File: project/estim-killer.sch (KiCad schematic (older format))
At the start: 3 parts

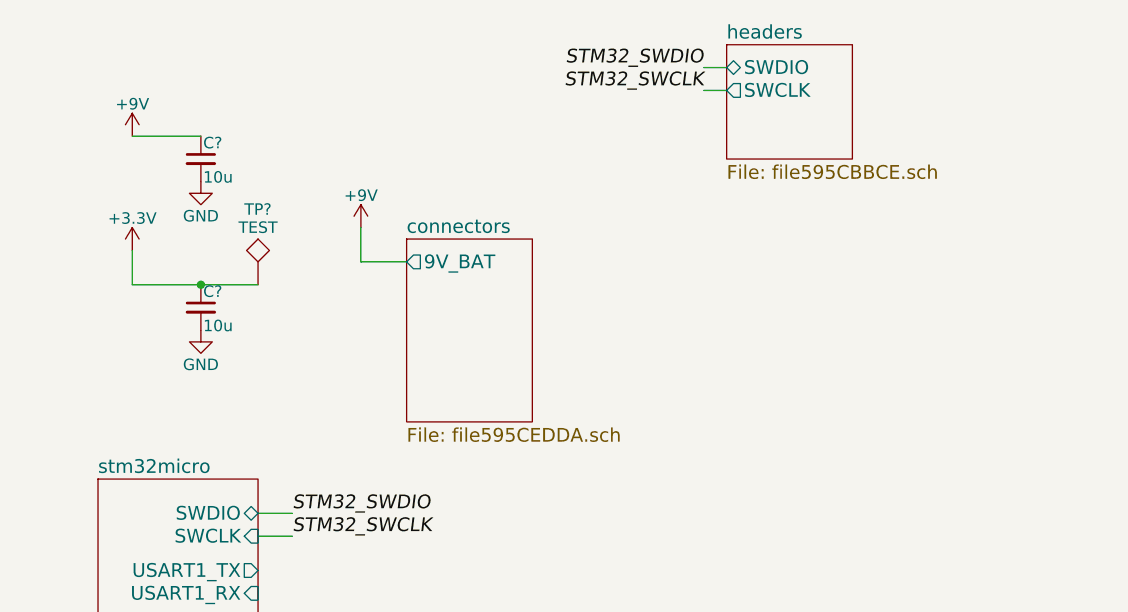
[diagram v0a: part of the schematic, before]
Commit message: Added 9V -> 3.3V buck regulator (TPS560200).
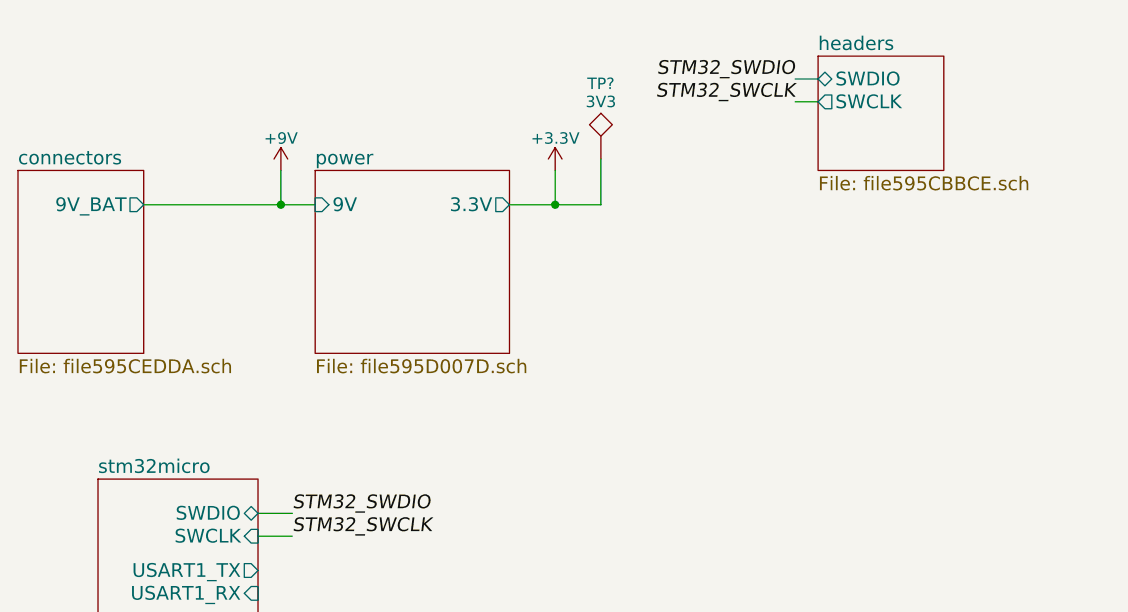
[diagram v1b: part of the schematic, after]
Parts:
- removed C?: 10u, Capacitors_SMD:C_0805, symbol C_Small
- removed C?: 10u, Capacitors_SMD:C_0603, symbol C_Small
- removed TP?: TEST, symbol TEST
- added TP?: 3V3, Measurement_Points:Measurement_Point_Round-SMD-Pad_Small, symbol TEST
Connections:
- net +3V3: now also TP?.1
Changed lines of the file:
@@
 LIBS:valves
 LIBS:estim-killer
+LIBS:estim-killer-cache
 EELAYER 25 0
 EELAYER END
 $Descr A4 11693 8268
 encoding utf-8
-Sheet 1 4
+Sheet 1 5
 Title ""
 Date ""
@@
 Comment4 ""
 $EndDescr
-$Comp
-L +9V #PWR?
-U 1 1 595C7B7C
-P 1350 1200
-F 0 "#PWR?" H 1350 1050 50  0001 C CNN
-F 1 "+9V" H 1350 1340 50  0000 C CNN
-F 2 "" H 1350 1200 50  0001 C CNN
-F 3 "" H 1350 1200 50  0001 C CNN
-	1    1350 1200
-	1    0    0    -1
-$EndComp
-$Comp
-L +3.3V #PWR?
-U 1 1 595C836F
-P 1350 1700
-F 0 "#PWR?" H 1350 1550 50  0001 C CNN
-F 1 "+3.3V" H 1350 1840 50  0000 C CNN
-F 2 "" H 1350 1700 50  0001 C CNN
-F 3 "" H 1350 1700 50  0001 C CNN
-	1    1350 1700
-	1    0    0    -1
-$EndComp
-$Comp
-L C_Small C?
-U 1 1 595C83A0
-P 1650 1300
-F 0 "C?" H 1660 1370 50  0000 L CNN
-F 1 "10u" H 1660 1220 50  0000 L CNN
-F 2 "Capacitors_SMD:C_0805" H 1650 1300 50  0001 C CNN
-F 3 "" H 1650 1300 50  0001 C CNN
-	1    1650 1300
-	1    0    0    -1
-$EndComp
-$Comp
-L GND #PWR?
-U 1 1 595C83DB
-P 1650 1400
-F 0 "#PWR?" H 1650 1150 50  0001 C CNN
-F 1 "GND" H 1650 1250 50  0000 C CNN
-F 2 "" H 1650 1400 50  0001 C CNN
-F 3 "" H 1650 1400 50  0001 C CNN
-	1    1650 1400
-	1    0    0    -1
-$EndComp
-Wire Wire Line
-	1350 1200 1650 1200
-$Comp
-L C_Small C?
-U 1 1 595C8416
-P 1650 1950
-F 0 "C?" H 1660 2020 50  0000 L CNN
-F 1 "10u" H 1660 1870 50  0000 L CNN
-F 2 "Capacitors_SMD:C_0603" H 1650 1950 50  0001 C CNN
-F 3 "" H 1650 1950 50  0001 C CNN
-	1    1650 1950
-	1    0    0    -1
-$EndComp
-Wire Wire Line
-	1350 1700 1350 1850
-Wire Wire Line
-	1350 1850 1900 1850
-$Comp
-L GND #PWR?
-U 1 1 595C8472
-P 1650 2050
-F 0 "#PWR?" H 1650 1800 50  0001 C CNN
-F 1 "GND" H 1650 1900 50  0000 C CNN
-F 2 "" H 1650 2050 50  0001 C CNN
-F 3 "" H 1650 2050 50  0001 C CNN
-	1    1650 2050
-	1    0    0    -1
-$EndComp
 $Sheet
 S 1200 2700 700  1350
@@
 $EndSheet
 $Sheet
-S 3950 800  550  500
+S 4350 850  550  500
 U 595CBBCF
 F0 "headers" 60
 F1 "file595CBBCE.sch" 60
-F2 "SWDIO" B L 3950 900 60
-F3 "SWCLK" O L 3950 1000 60
+F2 "SWDIO" B L 4350 950 60
+F3 "SWCLK" O L 4350 1050 60
 $EndSheet
-Text Label 3850 900  2    60   Italic 0
+Text Label 4250 950  2    60   Italic 0
 STM32_SWDIO
-Text Label 3850 1000 2    60   Italic 0
+Text Label 4250 1050 2    60   Italic 0
 STM32_SWCLK
 Wire Wire Line
-	3850 1000 3950 1000
+	4250 1050 4350 1050
 Wire Wire Line
-	3850 900  3950 900
+	4250 950  4350 950
 Text Label 2050 2850 0    60   Italic 0
 STM32_SWDIO
@@
 	1900 2950 2050 2950
 $Sheet
-S 2550 1650 550  800
+S 850  1350 550  800
 U 595CEDDB
 F0 "connectors" 60
 F1 "file595CEDDA.sch" 60
-F2 "9V_BAT" O L 2550 1750 60
+F2 "9V_BAT" O R 1400 1500 60
 $EndSheet
-$Comp
-L TEST TP?
-U 1 1 595CF833
-P 1900 1850
-F 0 "TP?" H 1900 2150 50  0000 C BNN
-F 1 "TEST" H 1900 2100 50  0000 C CNN
-F 2 "" H 1900 1850 50  0001 C CNN
-F 3 "" H 1900 1850 50  0001 C CNN
-	1    1900 1850
-	1    0    0    -1
-$EndComp
-Connection ~ 1650 1850
+$Sheet
+S 2150 1350 850  800
+U 595D007E
+F0 "power" 60
+F1 "file595D007D.sch" 60
+F2 "3.3V" O R 3000 1500 60
+F3 "9V" I L 2150 1500 60
+$EndSheet
+Wire Wire Line
+	1400 1500 2150 1500
 $Comp
 L +9V #PWR?
-U 1 1 595CFAF7
-P 2350 1600
-F 0 "#PWR?" H 2350 1450 50  0001 C CNN
-F 1 "+9V" H 2350 1740 50  0000 C CNN
-F 2 "" H 2350 1600 50  0001 C CNN
-F 3 "" H 2350 1600 50  0001 C CNN
-	1    2350 1600
+U 1 1 595D15BF
+P 2000 1350
+F 0 "#PWR?" H 2000 1200 50  0001 C CNN
+F 1 "+9V" H 2000 1490 50  0000 C CNN
+F 2 "" H 2000 1350 50  0001 C CNN
+F 3 "" H 2000 1350 50  0001 C CNN
+	1    2000 1350
 	1    0    0    -1
 $EndComp
 Wire Wire Line
-	2350 1600 2350 1750
+	2000 1350 2000 1500
+Connection ~ 2000 1500
+$Comp
+L +3.3V #PWR?
+U 1 1 595D18DD
+P 3200 1350
+F 0 "#PWR?" H 3200 1200 50  0001 C CNN
+F 1 "+3.3V" H 3200 1490 50  0000 C CNN
+F 2 "" H 3200 1350 50  0001 C CNN
+F 3 "" H 3200 1350 50  0001 C CNN
+	1    3200 1350
+	1    0    0    -1
+$EndComp
+$Comp
+L TEST TP?
+U 1 1 595D1C32
+P 3400 1300
+F 0 "TP?" H 3400 1600 50  0000 C BNN
+F 1 "3V3" H 3400 1550 50  0000 C CNN
+F 2 "Measurement_Points:Measurement_Point_Round-SMD-Pad_Small" H 3400 1300 50  0001 C CNN
+F 3 "" H 3400 1300 50  0001 C CNN
+	1    3400 1300
+	1    0    0    -1
+$EndComp
 Wire Wire Line
-	2350 1750 2550 1750
+	3000 1500 3400 1500
+Wire Wire Line
+	3400 1500 3400 1300
+Wire Wire Line
+	3200 1350 3200 1500
+Connection ~ 3200 1500
 $EndSCHEMATC

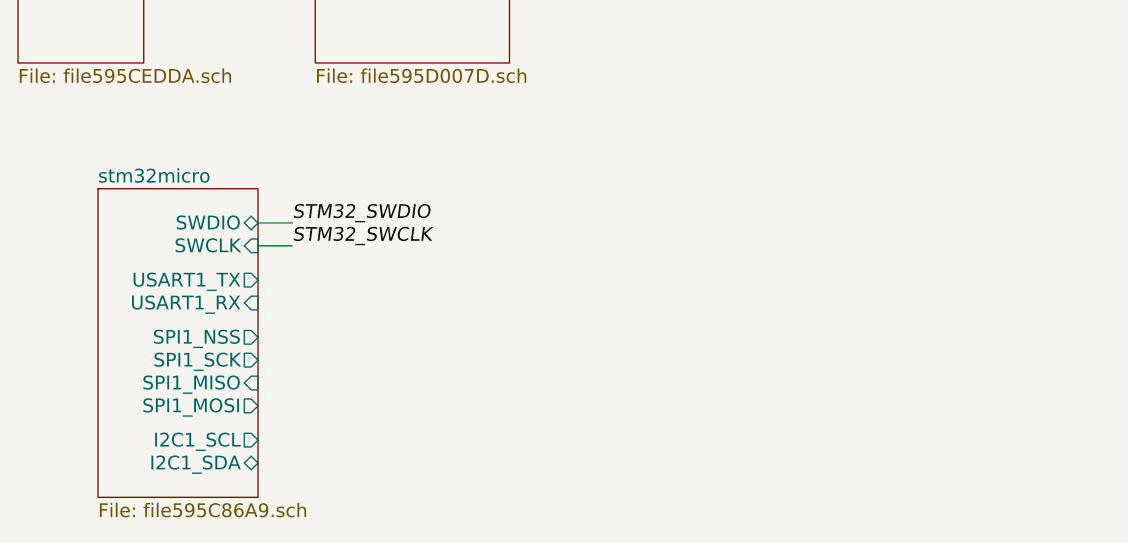
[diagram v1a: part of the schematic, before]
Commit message: Add AD5689R dual-channel DAC to schematic.
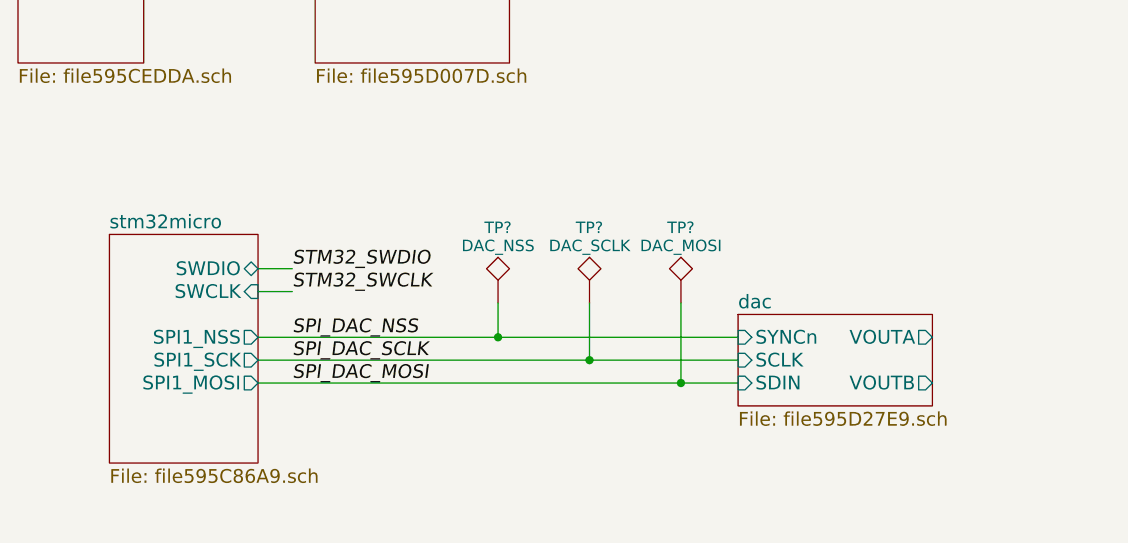
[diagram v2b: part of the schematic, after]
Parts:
- added TP?: DAC_NSS, Measurement_Points:Measurement_Point_Round-SMD-Pad_Small, symbol TEST
- added TP?: DAC_SCLK, Measurement_Points:Measurement_Point_Round-SMD-Pad_Small, symbol TEST
- added TP?: DAC_MOSI, Measurement_Points:Measurement_Point_Round-SMD-Pad_Small, symbol TEST
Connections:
- new net SPI_DAC_MOSI: TP?.1
- new net SPI_DAC_NSS: TP?.1
- new net SPI_DAC_SCLK: TP?.1
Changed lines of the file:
@@
 $Descr A4 11693 8268
 encoding utf-8
-Sheet 1 5
+Sheet 1 6
 Title ""
 Date ""
@@
 $EndDescr
 $Sheet
-S 1200 2700 700  1350
+S 1250 2900 650  1000
 U 595C86AA
 F0 "stm32micro" 60
 F1 "file595C86A9.sch" 60
-F2 "SWDIO" B R 1900 2850 60
-F3 "SWCLK" I R 1900 2950 60
-F4 "USART1_TX" O R 1900 3100 60
-F5 "USART1_RX" I R 1900 3200 60
-F6 "SPI1_NSS" O R 1900 3350 60
-F7 "SPI1_SCK" O R 1900 3450 60
-F8 "SPI1_MISO" I R 1900 3550 60
-F9 "SPI1_MOSI" O R 1900 3650 60
-F10 "I2C1_SCL" O R 1900 3800 60
-F11 "I2C1_SDA" B R 1900 3900 60
+F2 "SWDIO" B R 1900 3050 60
+F3 "SWCLK" I R 1900 3150 60
+F4 "SPI1_NSS" O R 1900 3350 60
+F5 "SPI1_SCK" O R 1900 3450 60
+F6 "SPI1_MOSI" O R 1900 3550 60
 $EndSheet
 $Sheet
@@
 Wire Wire Line
 	4250 950  4350 950
-Text Label 2050 2850 0    60   Italic 0
+Text Label 2050 3050 0    60   Italic 0
 STM32_SWDIO
-Wire Wire Line
-	1900 2850 2050 2850
-Text Label 2050 2950 0    60   Italic 0
+Text Label 2050 3150 0    60   Italic 0
 STM32_SWCLK
-Wire Wire Line
-	1900 2950 2050 2950
 $Sheet
 S 850  1350 550  800
@@
 	1400 1500 2150 1500
 $Comp
-L +9V #PWR?
+L +9V #PWR01
 U 1 1 595D15BF
 P 2000 1350
-F 0 "#PWR?" H 2000 1200 50  0001 C CNN
+F 0 "#PWR01" H 2000 1200 50  0001 C CNN
 F 1 "+9V" H 2000 1490 50  0000 C CNN
 F 2 "" H 2000 1350 50  0001 C CNN
@@
 Connection ~ 2000 1500
 $Comp
-L +3.3V #PWR?
+L +3.3V #PWR02
 U 1 1 595D18DD
 P 3200 1350
-F 0 "#PWR?" H 3200 1200 50  0001 C CNN
+F 0 "#PWR02" H 3200 1200 50  0001 C CNN
 F 1 "+3.3V" H 3200 1490 50  0000 C CNN
 F 2 "" H 3200 1350 50  0001 C CNN
@@
 	3200 1350 3200 1500
 Connection ~ 3200 1500
+$Sheet
+S 4000 3250 850  400
+U 595D27EA
+F0 "dac" 60
+F1 "file595D27E9.sch" 60
+F2 "VOUTA" O R 4850 3350 60
+F3 "VOUTB" O R 4850 3550 60
+F4 "SDIN" I L 4000 3550 60
+F5 "SYNCn" I L 4000 3350 60
+F6 "SCLK" I L 4000 3450 60
+$EndSheet
+Wire Wire Line
+	1900 3350 4000 3350
+Text Label 2050 3350 0    60   Italic 0
+SPI_DAC_NSS
+Wire Wire Line
+	1900 3450 4000 3450
+Text Label 2050 3450 0    60   Italic 0
+SPI_DAC_SCLK
+Text Label 2050 3550 0    60   Italic 0
+SPI_DAC_MOSI
+Wire Wire Line
+	1900 3550 4000 3550
+$Comp
+L TEST TP?
+U 1 1 595D5014
+P 2950 3200
+F 0 "TP?" H 2950 3500 50  0000 C BNN
+F 1 "DAC_NSS" H 2950 3450 50  0000 C CNN
+F 2 "Measurement_Points:Measurement_Point_Round-SMD-Pad_Small" H 2950 3200 50  0001 C CNN
+F 3 "" H 2950 3200 50  0001 C CNN
+	1    2950 3200
+	1    0    0    -1
+$EndComp
+$Comp
+L TEST TP?
+U 1 1 595D521E
+P 3350 3200
+F 0 "TP?" H 3350 3500 50  0000 C BNN
+F 1 "DAC_SCLK" H 3350 3450 50  0000 C CNN
+F 2 "Measurement_Points:Measurement_Point_Round-SMD-Pad_Small" H 3350 3200 50  0001 C CNN
+F 3 "" H 3350 3200 50  0001 C CNN
+	1    3350 3200
+	1    0    0    -1
+$EndComp
+$Comp
+L TEST TP?
+U 1 1 595D560A
+P 3750 3200
+F 0 "TP?" H 3750 3500 50  0000 C BNN
+F 1 "DAC_MOSI" H 3750 3450 50  0000 C CNN
+F 2 "Measurement_Points:Measurement_Point_Round-SMD-Pad_Small" H 3750 3200 50  0001 C CNN
+F 3 "" H 3750 3200 50  0001 C CNN
+	1    3750 3200
+	1    0    0    -1
+$EndComp
+Wire Wire Line
+	2950 3200 2950 3350
+Connection ~ 2950 3350
+Wire Wire Line
+	3350 3200 3350 3450
+Connection ~ 3350 3450
+Wire Wire Line
+	3750 3200 3750 3550
+Connection ~ 3750 3550
+Wire Wire Line
+	1900 3050 2050 3050
+Wire Wire Line
+	2050 3150 1900 3150
 $EndSCHEMATC
